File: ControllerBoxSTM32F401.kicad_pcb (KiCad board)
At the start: 2 copper layers, 115.3 x 110.7 mm, 56 parts, among them SW1 Switch, SW10 Switch, SW11 Switch, SW12 Switch, SW13 Switch, SW14 Switch, SW15 Switch, SW16 Switch, SW17 Switch, SW18 Switch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

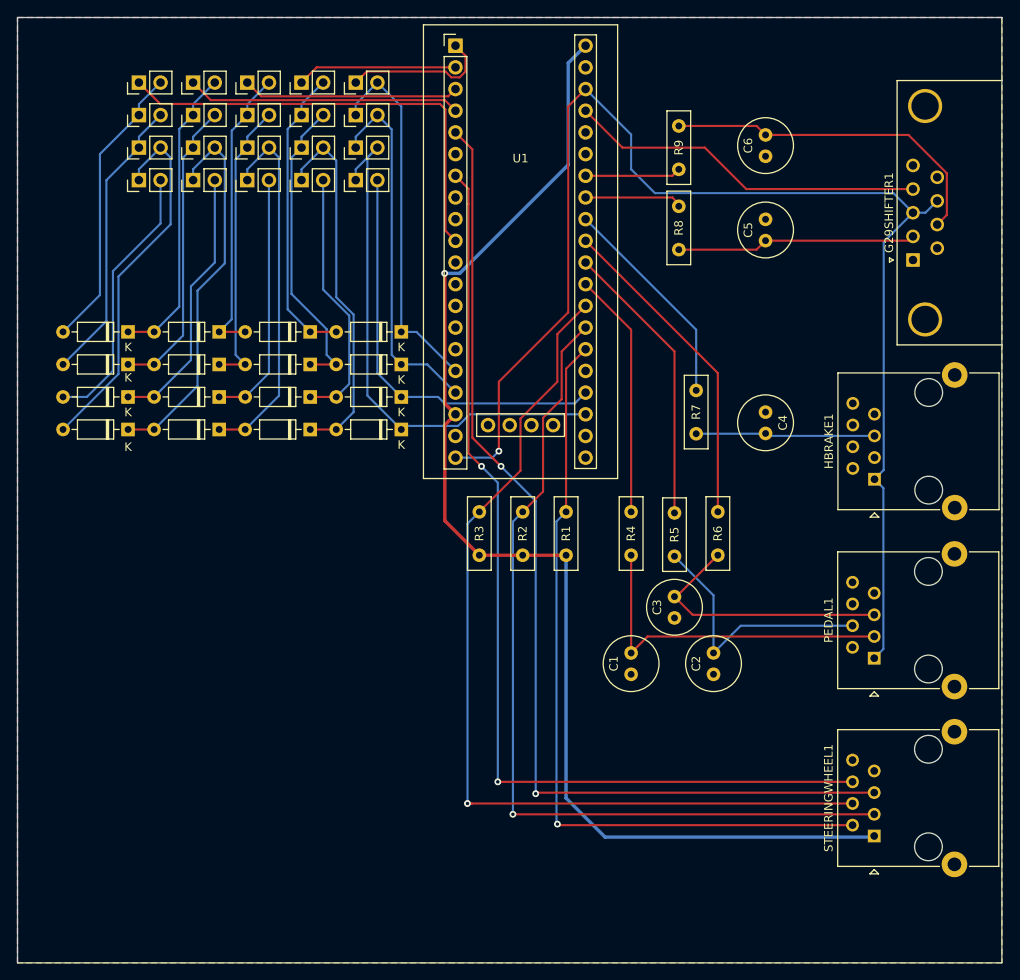
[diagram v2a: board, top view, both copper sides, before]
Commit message: fix v1 and make it smaller
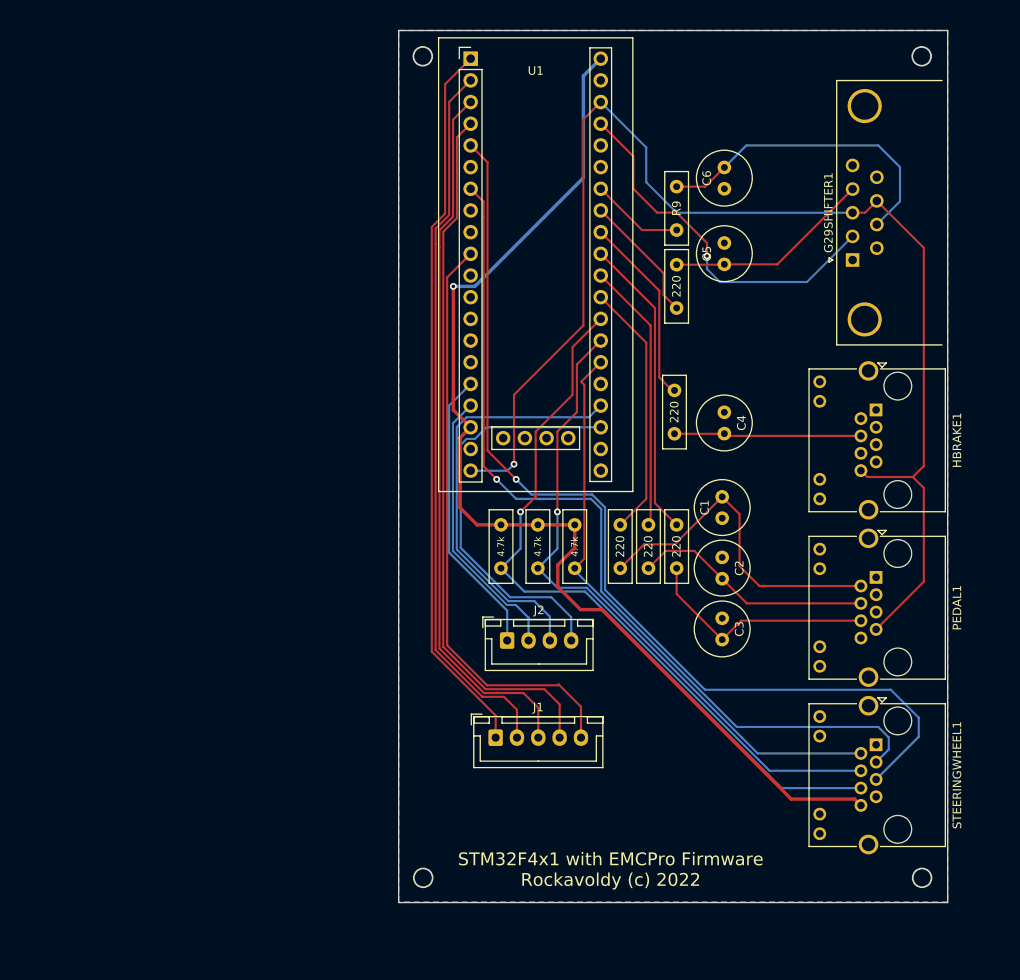
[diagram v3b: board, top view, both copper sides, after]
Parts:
- removed D1, D10, D11, D12, D13, D14, D15, D16, D2, D3, D4, D5, D6, D7, D8, D9: 1N4148, Diode_THT:D_DO-35_SOD27_P7.62mm_Horizontal
- removed SW1, SW10, SW11, SW12, SW13, SW14, SW15, SW16, SW17, SW18, SW19, SW2, SW20, SW3, SW4, SW5, SW6, SW7, SW8, SW9: Switch, Connector_PinHeader_2.54mm:PinHeader_1x02_P2.54mm_Vertical
- added J1: BTNROW, Connector_JST:JST_XH_B5B-XH-A_1x05_P2.50mm_Vertical, F.Cu at (94.4, 138.2)
- added J2: BTNCOL, Connector_JST:JST_XH_B4B-XH-A_1x04_P2.50mm_Vertical, F.Cu at (95.7, 126.8)
- HBRAKE1, PEDAL1, STEERINGWHEEL1: footprint Connector_RJ:RJ45_Ninigi_GE -> Connector_RJ:RJ45_Amphenol_RJHSE538X
- moved C1 21.2 mm to (120.9, 110.0)
- moved C2 13.7 mm to (120.9, 117.1), turned to -90 degrees
- moved STEERINGWHEEL1 10.7 mm to (138.9, 139.0), turned to -90 degrees
- moved PEDAL1 9.47 mm to (138.9, 119.4), turned to -90 degrees
- moved HBRAKE1 8.12 mm to (138.9, 99.8), turned to -90 degrees
- moved R9 7.12 mm to (115.6, 73.7)
- moved G29SHIFTER1 7.08 mm to (136.2, 82.3)
- moved C6 6.15 mm to (121.2, 73.9)
- moved C3 5.59 mm to (120.9, 124.2), turned to -90 degrees
- moved C5 5.57 mm to (121.2, 80.3)
- moved R6 5.06 mm to (115.6, 118.4)
- moved C4 4.83 mm to (121.2, 100.1)
- moved R3 4.37 mm to (95.0, 113.3), turned to -90 degrees
- moved R2 3.98 mm to (99.3, 113.3), turned to -90 degrees
- moved R1 3.70 mm to (103.6, 113.3), turned to -90 degrees
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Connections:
- G29SHIFTER1 pad 0: GND -> (no net)
- G29SHIFTER1 pad 2: SHIFTER X -> REVERSE
- G29SHIFTER1 pad 4: REVERSE -> SHIFTER X
- HBRAKE1 pad 1: VCC 3.3V -> GND
- HBRAKE1 pad 4: unconnected-(HBRAKE1-Pad4) -> HBRAKE
- HBRAKE1 pad 5: HBRAKE -> unconnected-(HBRAKE1-Pad5)
- HBRAKE1 pad 8: GND -> VCC 3.3V
- HBRAKE1 pad SH: GND -> (no net)
- PEDAL1 pad 1: VCC 3.3V -> GND
- PEDAL1 pad 2: unconnected-(PEDAL1-Pad2) -> ACCEL
- PEDAL1 pad 3: ACCEL -> unconnected-(PEDAL1-Pad3)
- PEDAL1 pad 5: CLUTCH -> unconnected-(PEDAL1-Pad5)
- PEDAL1 pad 6: unconnected-(PEDAL1-Pad6) -> CLUTCH
- PEDAL1 pad 7: unconnected-(PEDAL1-Pad7) -> VCC 3.3V
- PEDAL1 pad 8: GND -> unconnected-(PEDAL1-Pad8)
- PEDAL1 pad SH: GND -> (no net)
- STEERINGWHEEL1 pad 1: VCC 5V -> GND
- STEERINGWHEEL1 pad 3: ENC B -> DIR
- STEERINGWHEEL1 pad 4: ENC Z -> ENC B
- STEERINGWHEEL1 pad 6: DIR -> ENC Z
- STEERINGWHEEL1 pad 8: GND -> VCC 5V
- STEERINGWHEEL1 pad SH: GND -> (no net)
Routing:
- net BTN_ROW1: track 17.5 -> 84.5 mm
- net BTN_ROW2: track 18.8 -> 84.1 mm
- net BTN_ROW3: track 25.4 -> 83.5 mm
- net BTN_ROW4: track 32.1 -> 82.9 mm
- net Net-(SW14-Pad2): track 44.8 -> 0.00 mm
- net Net-(SW15-Pad2): track 43.6 -> 0.00 mm
- net Net-(SW12-Pad2): track 43.2 -> 0.00 mm
- net Net-(SW13-Pad2): track 43.1 -> 0.00 mm
- net Net-(SW12-Pad1): track 36.0 -> 0.00 mm
- net Net-(SW14-Pad1): track 35.2 -> 0.00 mm
- net Net-(SW4-Pad2): track 35.2 -> 0.00 mm
- net Net-(SW2-Pad2): track 35.1 -> 0.00 mm
- net Net-(SW3-Pad2): track 34.7 -> 0.00 mm
- net Net-(SW13-Pad1): track 34.3 -> 0.00 mm
- net Net-(SW10-Pad2): track 33.9 -> 0.00 mm
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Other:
- board size 115.3 x 110.7 mm -> 64.3 x 102.2 mm
- board text added: "STM32F4x1 with EMCPro Firmware Rockavoldy (c) 2022"

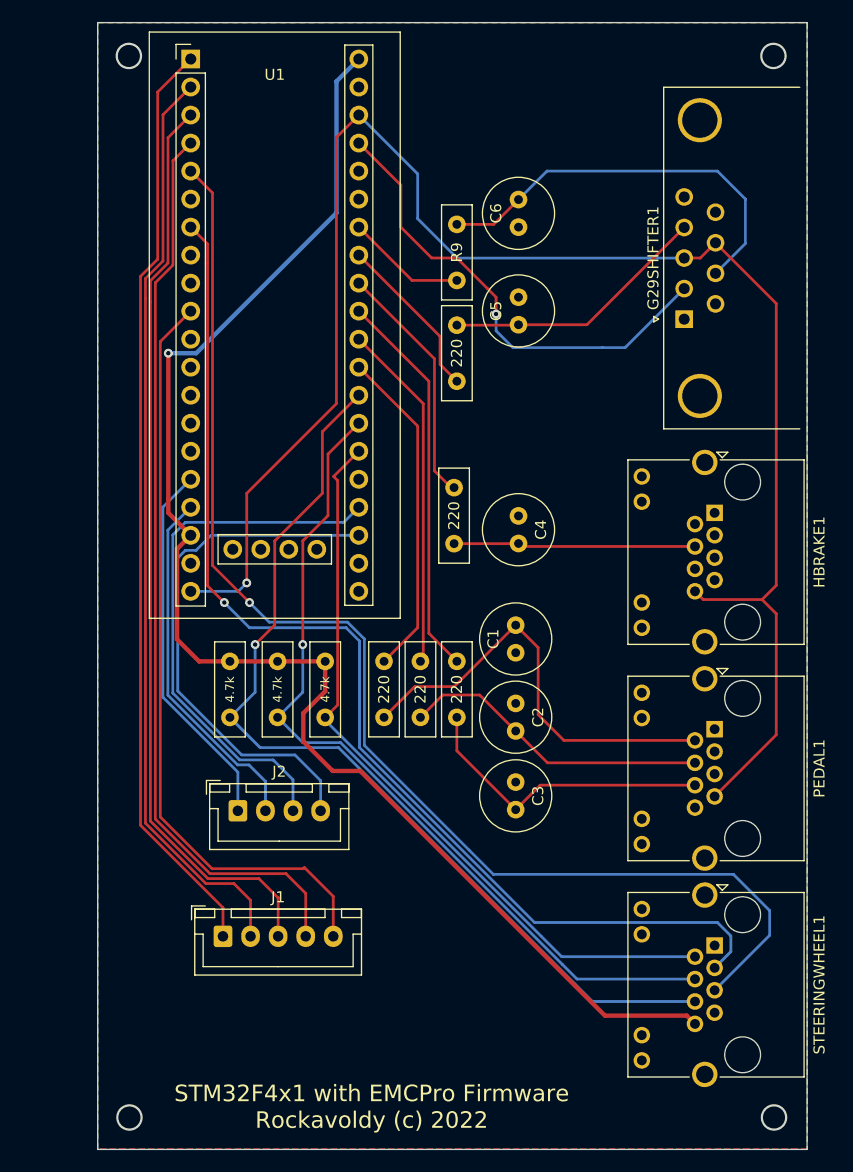
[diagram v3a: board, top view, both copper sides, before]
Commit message: change component to SMD, and lowering the footprint to <100mm
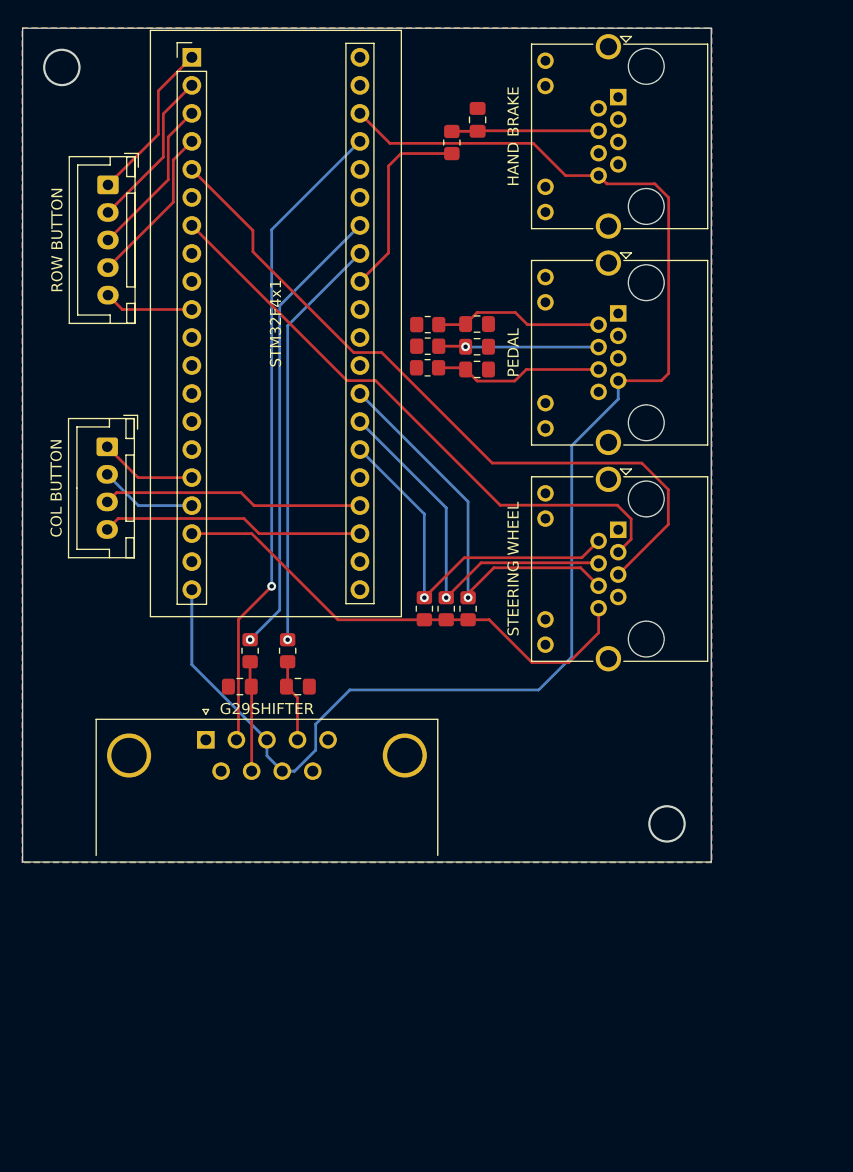
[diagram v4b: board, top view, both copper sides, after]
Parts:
- C1, C2, C3, C4, C5, C6: footprint Capacitor_THT:C_Radial_D6.3mm_H7.0mm_P2.50mm -> Capacitor_SMD:C_0805_2012Metric_Pad1.18x1.45mm_HandSolder
- HBRAKE1: value RJ45 -> HAND BRAKE
- J1: value BTNROW -> ROW BUTTON
- J2: value BTNCOL -> COL BUTTON
- PEDAL1: value RJ45 -> PEDAL
- R1, R2, R3, R4, R5, R6, R7, R8, R9: footprint Resistor_THT:R_Box_L8.4mm_W2.5mm_P5.08mm -> Resistor_SMD:R_0805_2012Metric_Pad1.20x1.40mm_HandSolder
- STEERINGWHEEL1: value RJ45 -> STEERING WHEEL
- U1: footprint Footprints:YAAJ_WeAct_BlackPill_SWD_2 -> Footprints:YAAJ_WeAct_BlackPill_2
- moved J1 68.9 mm to (83.9, 70.1), turned to -90 degrees
- moved G29SHIFTER 57.8 mm to (92.8, 120.4), turned to 0 degrees
- moved C6 48.7 mm to (95.9, 115.6), turned to 0 degrees
- moved R9 43.0 mm to (96.8, 112.3), turned to 90 degrees
- moved C5 40.6 mm to (101.2, 115.6), turned to 180 degrees
- moved STEERINGWHEEL1 38.7 mm to (130.2, 101.3)
- moved HBRAKE1 38.7 mm to (130.2, 62.1)
- moved PEDAL1 38.7 mm to (130.2, 81.7)
- moved C3 37.6 mm to (117.4, 86.8), turned to 180 degrees
- moved R7 36.4 mm to (115.1, 66.2), turned to -90 degrees
- moved C4 36.1 mm to (117.4, 64.2)
- moved R4 35.8 mm to (112.9, 82.8), turned to 180 degrees
- moved J2 35.1 mm to (83.9, 93.8), turned to -90 degrees
- moved R5 33.7 mm to (112.9, 84.7), turned to 180 degrees
- moved R8 33.3 mm to (100.2, 112.3), turned to 90 degrees
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- renumbered G29SHIFTER1 to G29SHIFTER
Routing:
- net VCC 5V: track 131.1 -> 45.1 mm, vias 1 -> 0
- net BTN_ROW1: track 84.5 -> 14.7 mm
- net BTN_ROW2: track 84.1 -> 14.7 mm
- net BTN_ROW3: track 83.5 -> 14.6 mm
- net BTN_ROW4: track 82.9 -> 14.6 mm
- net BTN_ROW5: track 69.4 -> 8.14 mm
- net ENC Z: track 86.9 -> 36.4 mm
- net PWM: track 115.0 -> 65.9 mm, vias 1 -> 0
- net DIR: track 102.9 -> 54.3 mm, vias 1 -> 0
- net ENC B: track 77.4 -> 34.4 mm
- net Net-(R6-Pad2): track 35.4 -> 0.00 mm
- net ENC A: track 68.4 -> 33.8 mm, vias 0 -> 1
- net Net-(R5-Pad2): track 31.7 -> 0.00 mm
- net Net-(R9-Pad2): track 10.9 -> 41.7 mm, vias 0 -> 1
- net Net-(R4-Pad2): track 30.1 -> 0.00 mm
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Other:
- board size 64.3 x 102.2 mm -> 62.4 x 75.6 mm
- board text removed: "STM32F4x1 with EMCPro Firmware Rockavoldy (c) 2022"
